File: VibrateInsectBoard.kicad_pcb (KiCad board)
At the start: 2 copper layers, 23.3 x 51.2 mm, 3 parts, among them M1 Vibrator, SW1 SW_SPDT

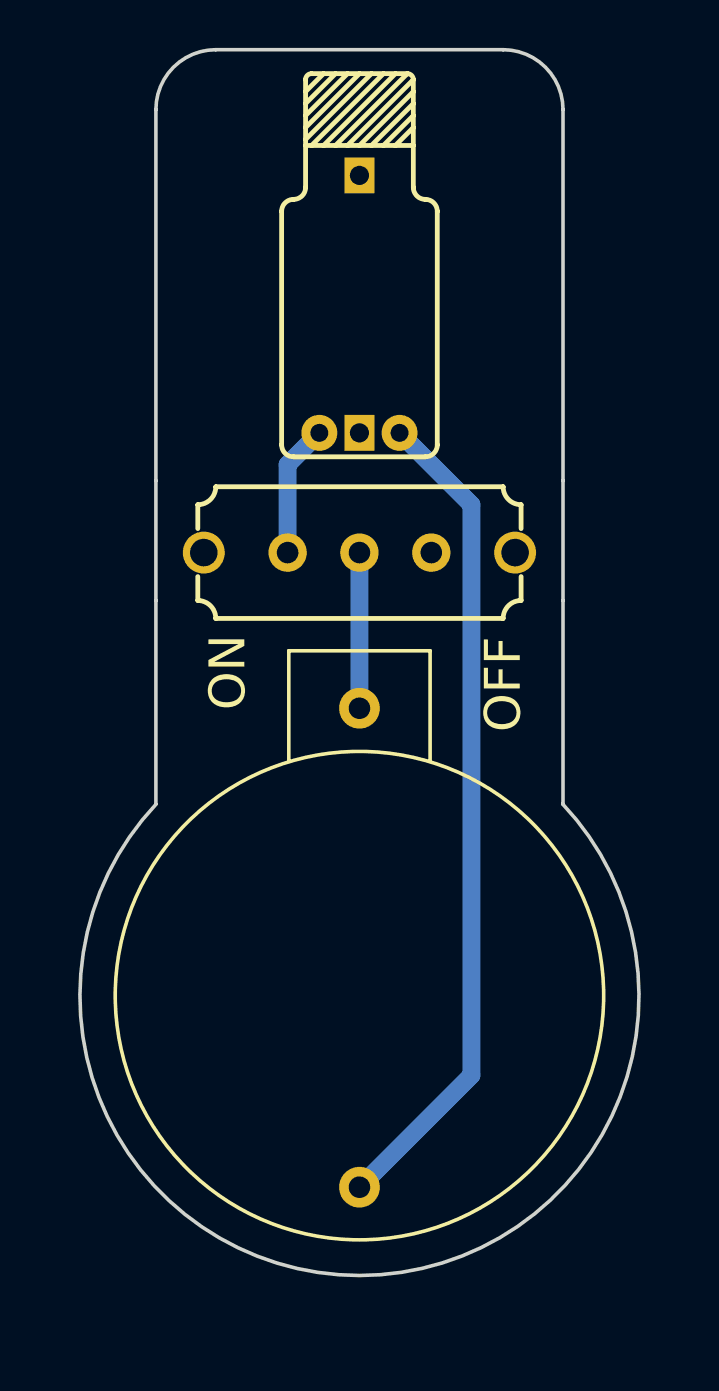
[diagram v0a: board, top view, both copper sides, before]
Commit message: Fix footprint and resize PCB. All done.
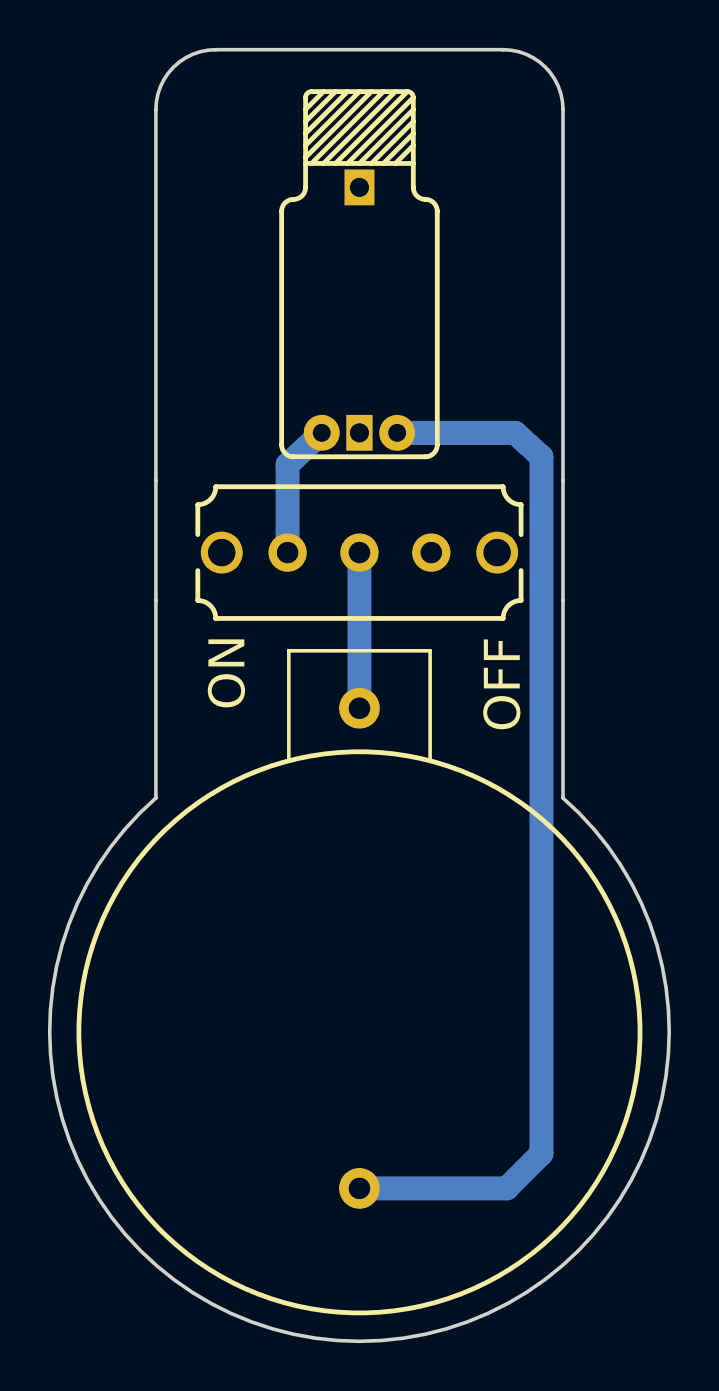
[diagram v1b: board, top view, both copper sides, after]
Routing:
- net Net-(BT1-Pad2): track 34.7 -> 43.7 mm
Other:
- board size 23.3 x 51.2 mm -> 25.9 x 53.9 mm
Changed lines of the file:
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@@
     (thickness 1.6)
     (drawings 12)
-    (tracks 6)
+    (tracks 8)
     (zones 0)
     (modules 3)
@@
   (page A4)
   (layers
-    (0 F.Cu signal hide)
+    (0 F.Cu signal)
     (31 B.Cu signal)
     (32 B.Adhes user)
@@
   )
   (setup
-    (last_trace_width 0.75)
+    (last_trace_width 0.25)
     (user_trace_width 0.5)
     (user_trace_width 0.6)
@@
       (usegerberadvancedattributes false)
       (creategerberjobfile false)
+      (gerberprecision 5)
       (excludeedgelayer true)
       (linewidth 0.100000)
@@
       (outputformat 1)
       (mirror false)
-      (drillshape 1)
+      (drillshape 0)
       (scaleselection 1)
-      (outputdirectory ""))
+      (outputdirectory "gerber/"))
   )
   (net 0 "")
@@
       (effects (font (size 1 1) (thickness 0.15)))
     )
-    (fp_circle (center 12 0) (end 22 2) (layer F.SilkS) (width 0.15))
+    (fp_circle (center 13.533734 0) (end 24.007912 5.25) (layer F.SilkS) (width 0.2))
     (fp_line (start -2.4 -2.95) (end -2.4 2.95) (layer F.SilkS) (width 0.15))
-    (fp_line (start -2.4 2.95) (end 2.2 2.95) (layer F.SilkS) (width 0.15))
-    (fp_line (start -2.4 -2.95) (end 2.2 -2.95) (layer F.SilkS) (width 0.15))
-    (pad 2 thru_hole circle (at 20 0 270) (size 1.7 1.7) (drill 0.9) (layers *.Cu *.Mask)
+    (fp_line (start -2.4 2.95) (end 2.15 2.95) (layer F.SilkS) (width 0.15))
+    (fp_line (start -2.4 -2.95) (end 2.15 -2.95) (layer F.SilkS) (width 0.15))
+    (pad 2 thru_hole circle (at 20.05 0 270) (size 1.7 1.7) (drill 0.9) (layers *.Cu *.Mask)
       (net 2 "Net-(BT1-Pad2)"))
     (pad 1 thru_hole circle (at 0 0 270) (size 1.7 1.7) (drill 0.9) (layers *.Cu *.Mask)
@@
       (effects (font (size 1 1) (thickness 0.15)))
     )
-    (fp_line (start 6.75 -2) (end 6.75 -1) (layer F.SilkS) (width 0.2))
-    (fp_line (start 6.75 1) (end 6.75 2) (layer F.SilkS) (width 0.2))
-    (fp_line (start -6.75 1) (end -6.75 2) (layer F.SilkS) (width 0.2))
+    (fp_line (start 6.75 -2) (end 6.75 -0.75) (layer F.SilkS) (width 0.2))
+    (fp_line (start 6.75 0.75) (end 6.75 2) (layer F.SilkS) (width 0.2))
+    (fp_line (start -6.75 0.75) (end -6.75 2) (layer F.SilkS) (width 0.2))
     (fp_arc (start 6.75 -2.75) (end 6 -2.75) (angle -90) (layer F.SilkS) (width 0.2))
     (fp_arc (start -6.75 -2.75) (end -6.75 -2) (angle -90) (layer F.SilkS) (width 0.2))
@@
     (fp_line (start -6 2.75) (end 6 2.75) (layer F.SilkS) (width 0.2))
     (fp_line (start -6 -2.75) (end 6 -2.75) (layer F.SilkS) (width 0.2))
-    (fp_line (start -6.75 -2) (end -6.75 -1) (layer F.SilkS) (width 0.2))
-    (pad MP thru_hole circle (at 6.5 0) (size 1.75 1.75) (drill 1.15) (layers *.Cu *.Mask))
-    (pad MP thru_hole circle (at -6.5 0) (size 1.75 1.75) (drill 1.15) (layers *.Cu *.Mask))
+    (fp_line (start -6.75 -2) (end -6.75 -0.75) (layer F.SilkS) (width 0.2))
+    (pad MP thru_hole circle (at 5.75 0) (size 1.75 1.75) (drill 1.15) (layers *.Cu *.Mask))
+    (pad MP thru_hole circle (at -5.75 0) (size 1.75 1.75) (drill 1.15) (layers *.Cu *.Mask))
     (pad 3 thru_hole circle (at 3 0) (size 1.6 1.6) (drill 0.9) (layers *.Cu *.Mask)
       (net 4 "Net-(SW1-Pad3)"))
@@
     (fp_arc (start 2.75 -4.75) (end 2.25 -4.75) (angle -90) (layer F.SilkS) (width 0.2))
     (fp_arc (start -2.75 -4.75) (end -2.75 -4.25) (angle -90) (layer F.SilkS) (width 0.2))
-    (fp_arc (start -2 -9.25) (end -2 -9.5) (angle -90) (layer F.SilkS) (width 0.2))
-    (fp_arc (start 2 -9.25) (end 2.25 -9.25) (angle -90) (layer F.SilkS) (width 0.2))
-    (fp_line (start 1.5 -6.5) (end 2.25 -7.25) (layer F.SilkS) (width 0.2))
-    (fp_line (start 1 -6.5) (end 2.25 -7.75) (layer F.SilkS) (width 0.2))
-    (fp_line (start 0.5 -6.5) (end 2.25 -8.25) (layer F.SilkS) (width 0.2))
-    (fp_line (start 0 -6.5) (end 2.25 -8.75) (layer F.SilkS) (width 0.2))
-    (fp_line (start -0.5 -6.5) (end 2.25 -9.25) (layer F.SilkS) (width 0.2))
-    (fp_line (start -1 -6.5) (end 2 -9.5) (layer F.SilkS) (width 0.2))
-    (fp_line (start -1.5 -6.5) (end 1.5 -9.5) (layer F.SilkS) (width 0.2))
-    (fp_line (start -2 -6.5) (end 1 -9.5) (layer F.SilkS) (width 0.2))
-    (fp_line (start -2.25 -6.75) (end 0.5 -9.5) (layer F.SilkS) (width 0.2))
-    (fp_line (start -2.25 -7.25) (end 0 -9.5) (layer F.SilkS) (width 0.2))
-    (fp_line (start -2.25 -7.75) (end -0.5 -9.5) (layer F.SilkS) (width 0.2))
-    (fp_line (start -2.25 -8.25) (end -1 -9.5) (layer F.SilkS) (width 0.2))
-    (fp_line (start -2.25 -8.75) (end -1.5 -9.5) (layer F.SilkS) (width 0.2))
-    (fp_line (start -2.25 -6.5) (end 2.25 -6.5) (layer F.SilkS) (width 0.2))
-    (fp_line (start 2.25 -4.75) (end 2.25 -9.25) (layer F.SilkS) (width 0.2))
-    (fp_line (start -2.25 -4.75) (end -2.25 -9.25) (layer F.SilkS) (width 0.2))
+    (fp_arc (start -2 -8.5) (end -2 -8.75) (angle -90) (layer F.SilkS) (width 0.2))
+    (fp_arc (start 2 -8.5) (end 2.25 -8.5) (angle -90) (layer F.SilkS) (width 0.2))
+    (fp_line (start 1.5 -5.75) (end 2.25 -6.5) (layer F.SilkS) (width 0.2))
+    (fp_line (start 1 -5.75) (end 2.25 -7) (layer F.SilkS) (width 0.2))
+    (fp_line (start 0.5 -5.75) (end 2.25 -7.5) (layer F.SilkS) (width 0.2))
+    (fp_line (start 0 -5.75) (end 2.25 -8) (layer F.SilkS) (width 0.2))
+    (fp_line (start -0.5 -5.75) (end 2.25 -8.5) (layer F.SilkS) (width 0.2))
+    (fp_line (start -1 -5.75) (end 2 -8.75) (layer F.SilkS) (width 0.2))
+    (fp_line (start -1.5 -5.75) (end 1.5 -8.75) (layer F.SilkS) (width 0.2))
+    (fp_line (start -2 -5.75) (end 1 -8.75) (layer F.SilkS) (width 0.2))
+    (fp_line (start -2.25 -6) (end 0.5 -8.75) (layer F.SilkS) (width 0.2))
+    (fp_line (start -2.25 -6.5) (end 0 -8.75) (layer F.SilkS) (width 0.2))
+    (fp_line (start -2.25 -7) (end -0.5 -8.75) (layer F.SilkS) (width 0.2))
+    (fp_line (start -2.25 -7.5) (end -1 -8.75) (layer F.SilkS) (width 0.2))
+    (fp_line (start -2.25 -8) (end -1.5 -8.75) (layer F.SilkS) (width 0.2))
+    (fp_line (start -2.25 -5.75) (end 2.25 -5.75) (layer F.SilkS) (width 0.2))
+    (fp_line (start 2.25 -4.75) (end 2.25 -8.5) (layer F.SilkS) (width 0.2))
+    (fp_line (start -2.25 -4.75) (end -2.25 -8.5) (layer F.SilkS) (width 0.2))
     (fp_line (start 3.25 6) (end 3.25 -3.75) (layer F.SilkS) (width 0.2))
     (fp_line (start -3.25 6) (end -3.25 -3.75) (layer F.SilkS) (width 0.2))
-    (fp_line (start -2 -9.5) (end 2 -9.5) (layer F.SilkS) (width 0.2))
+    (fp_line (start -2 -8.75) (end 2 -8.75) (layer F.SilkS) (width 0.2))
     (fp_line (start -2.75 6.5) (end 2.75 6.5) (layer F.SilkS) (width 0.2))
-    (pad 2 thru_hole circle (at 1.675 5.5) (size 1.5 1.5) (drill 0.75) (layers *.Cu *.Mask)
+    (pad 2 thru_hole circle (at 1.575 5.5) (size 1.5 1.5) (drill 0.75) (layers *.Cu *.Mask)
       (net 2 "Net-(BT1-Pad2)"))
-    (pad 1 thru_hole circle (at -1.675 5.5) (size 1.5 1.5) (drill 0.75) (layers *.Cu *.Mask)
+    (pad 1 thru_hole circle (at -1.575 5.5) (size 1.5 1.5) (drill 0.75) (layers *.Cu *.Mask)
       (net 1 "Net-(M1-Pad1)"))
-    (pad MP thru_hole rect (at 0 -5.25) (size 1.25 1.5) (drill 0.8) (layers *.Cu *.Mask))
-    (pad MP thru_hole rect (at 0 5.5) (size 1.25 1.5) (drill 0.8) (layers *.Cu *.Mask))
-  )
+    (pad MP thru_hole rect (at 0 -4.75) (size 1.25 1.5) (drill 0.8) (layers *.Cu *.Mask))
+    (pad MP thru_hole rect (at 0 5.5) (size 1.1 1.5) (drill 0.8) (layers *.Cu *.Mask))
+  )
+  (gr_arc (start 164.999999 107.999999) (end 156.5 98.25) (angle -277.8364977) (layer Edge.Cuts) (width 0.15))
   (gr_text OFF (at 171 93.5 90) (layer F.SilkS)
     (effects (font (size 1.5 1.5) (thickness 0.3)))
@@
   (gr_line (start 173.5 85) (end 173.5 69.5) (layer Edge.Cuts) (width 0.15))
   (gr_line (start 156.5 85) (end 156.5 69.5) (layer Edge.Cuts) (width 0.15))
-  (gr_arc (start 165 106.514693) (end 156.500001 98.514694) (angle -266.6277184) (layer Edge.Cuts) (width 0.15))
-  (gr_line (start 173.5 90) (end 173.5 98.5) (layer Edge.Cuts) (width 0.15))
-  (gr_line (start 156.5 90) (end 156.5 98.5) (layer Edge.Cuts) (width 0.15))
+  (gr_line (start 173.5 90) (end 173.5 98.25) (layer Edge.Cuts) (width 0.15))
+  (gr_line (start 156.5 90) (end 156.5 98.25) (layer Edge.Cuts) (width 0.15))
   (gr_line (start 173.5 90) (end 173.5 85) (layer Edge.Cuts) (width 0.15))
   (gr_line (start 159 67) (end 171 67) (layer Edge.Cuts) (width 0.15))
   (gr_line (start 156.5 90) (end 156.5 85) (layer Edge.Cuts) (width 0.15))
-  (segment (start 162 84.325) (end 163.325 83) (width 0.75) (layer B.Cu) (net 1))
-  (segment (start 162 88) (end 162 84.325) (width 0.75) (layer B.Cu) (net 1))
-  (segment (start 169.675 109.825) (end 165 114.5) (width 0.75) (layer B.Cu) (net 2))
-  (segment (start 166.675 83) (end 169.675 86) (width 0.75) (layer B.Cu) (net 2))
-  (segment (start 169.675 86) (end 169.675 109.825) (width 0.75) (layer B.Cu) (net 2))
-  (segment (start 165 94.5) (end 165 88) (width 0.75) (layer B.Cu) (net 3))
+  (segment (start 162 84.325) (end 163.425 83) (width 1) (layer B.Cu) (net 1))
+  (segment (start 162 88) (end 162 84.325) (width 1) (layer B.Cu) (net 1))
+  (segment (start 171.15 114.55) (end 172.6 113.1) (width 1) (layer B.Cu) (net 2))
+  (segment (start 165 114.55) (end 171.15 114.55) (width 1) (layer B.Cu) (net 2))
+  (segment (start 172.6 113.1) (end 172.6 84) (width 1) (layer B.Cu) (net 2))
+  (segment (start 171.5 83) (end 166.575 83) (width 1) (layer B.Cu) (net 2))
+  (segment (start 172.6 84) (end 171.5 83) (width 1) (layer B.Cu) (net 2))
+  (segment (start 165 94.5) (end 165 88) (width 1) (layer B.Cu) (net 3))
 )
